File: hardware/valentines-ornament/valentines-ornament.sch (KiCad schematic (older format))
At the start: 17 parts, among them U1 ATtiny85-20SU

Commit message: Finished schematic capture; started PCB layout
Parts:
- added C1: 10uF, Capacitors_SMD:C_1206_HandSoldering, symbol Device:C
- added J1: AVR-ISP-6, Pin_Headers:Pin_Header_Straight_2x03_Pitch2.54mm_SMD, symbol Connector:AVR-ISP-6
- added R5: 10K, Resistors_SMD:R_1206_HandSoldering, symbol Device:R
- added SW1: SW_Push, Buttons_Switches_SMD:SW_SPST_EVQQ2, symbol Switch:SW_Push
- U1: footprint Package_SO:SOIJ-8_5.3x5.3mm_P1.27mm -> kicad-libs:SOIJ-8_5.3x5.3mm_P1.27mm
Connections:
- net RST: now reaches U1.1 (~RESET~/PB5)
- net RST: now also J1.5 (~RST)
- net at U1.2 (XTAL1/PB3): now also R3.2
- net at U1.3 (XTAL2/PB4): now also R4.2
- net GND: now reaches U1.4 (GND)
- net GND: now also C1.1, J1.6 (GND), R5.2
- net MOSI: now reaches U1.5 (AREF/PB0)
- net MOSI: now also R1.2, J1.4 (MOSI)
- net MISO: now reaches U1.6 (PB1)
- net MISO: now also R2.2, J1.1 (MISO)
- net SCK_BUTTON: now reaches U1.7 (PB2)
- net SCK_BUTTON: now also J1.3 (SCK), R5.1, SW1.2
- net +3V3: now reaches U1.8 (VCC)
- net +3V3: now also C1.2, J1.2 (VCC), SW1.1
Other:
- moved on the sheet: D1, D10, D11, D12, D2, D3, D4, D5, D6, D7, D8, D9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

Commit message: Add battery cell
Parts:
- added BT1: Battery_Cell, kicad-libs:CR2032-SMD, symbol Device:Battery_Cell
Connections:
- net +3V3: now also BT1.1 (+)
- net GND: now also BT1.2 (-)
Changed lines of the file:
@@
 	4700 3550 5200 3550
 $Comp
-L power:PWR_FLAG #FLG?
+L power:PWR_FLAG #FLG0101
 U 1 1 5C577048
 P 2150 4700
-F 0 "#FLG?" H 2150 4775 50  0001 C CNN
+F 0 "#FLG0101" H 2150 4775 50  0001 C CNN
 F 1 "PWR_FLAG" V 2150 4828 50  0000 L CNN
 F 2 "" H 2150 4700 50  0001 C CNN
@@
 Connection ~ 2150 4700
 $Comp
-L power:PWR_FLAG #FLG?
+L power:PWR_FLAG #FLG0102
 U 1 1 5C5770B0
 P 2150 5600
-F 0 "#FLG?" H 2150 5675 50  0001 C CNN
+F 0 "#FLG0102" H 2150 5675 50  0001 C CNN
 F 1 "PWR_FLAG" V 2150 5728 50  0000 L CNN
 F 2 "" H 2150 5600 50  0001 C CNN
@@
 $EndComp
 Connection ~ 2150 5600
+$Comp
+L Device:Battery_Cell BT1
+U 1 1 5C57A79D
+P 1800 2150
+F 0 "BT1" H 1918 2246 50  0000 L CNN
+F 1 "Battery_Cell" H 1918 2155 50  0000 L CNN
+F 2 "kicad-libs:CR2032-SMD" V 1800 2210 50  0001 C CNN
+F 3 "~" V 1800 2210 50  0001 C CNN
+	1    1800 2150
+	1    0    0    -1
+$EndComp
+$Comp
+L power:+3.3V #PWR0108
+U 1 1 5C57AA3C
+P 1800 1950
+F 0 "#PWR0108" H 1800 1800 50  0001 C CNN
+F 1 "+3.3V" H 1815 2123 50  0000 C CNN
+F 2 "" H 1800 1950 50  0001 C CNN
+F 3 "" H 1800 1950 50  0001 C CNN
+	1    1800 1950
+	1    0    0    -1
+$EndComp
+$Comp
+L power:GND #PWR0109
+U 1 1 5C57AAB4
+P 1800 2250
+F 0 "#PWR0109" H 1800 2000 50  0001 C CNN
+F 1 "GND" H 1805 2077 50  0000 C CNN
+F 2 "" H 1800 2250 50  0001 C CNN
+F 3 "" H 1800 2250 50  0001 C CNN
+	1    1800 2250
+	1    0    0    -1
+$EndComp
 $EndSCHEMATC

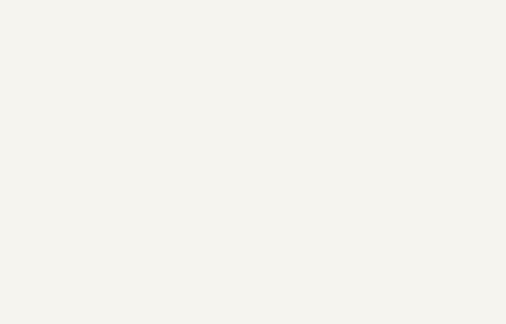
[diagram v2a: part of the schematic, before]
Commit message: Add heart solder mask logo, switch resistors to 0805
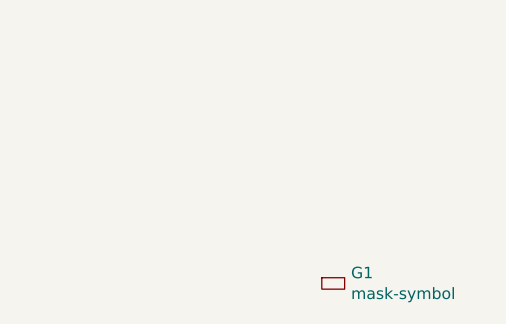
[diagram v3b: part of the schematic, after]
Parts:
- added G1: mask-symbol, kicad-libs:abstract-heart, symbol petezah:mask-symbol
- R1, R2, R3, R4, R5: footprint Resistors_SMD:R_1206_HandSoldering -> Resistors_SMD:R_0805_HandSoldering
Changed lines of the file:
@@
 F 0 "R1" V 5143 2350 50  0000 C CNN
 F 1 "270" V 5234 2350 50  0000 C CNN
-F 2 "Resistors_SMD:R_1206_HandSoldering" V 5280 2350 50  0001 C CNN
+F 2 "Resistors_SMD:R_0805_HandSoldering" V 5280 2350 50  0001 C CNN
 F 3 "~" H 5350 2350 50  0001 C CNN
 	1    5350 2350
@@
 F 0 "R2" V 5143 2750 50  0000 C CNN
 F 1 "270" V 5234 2750 50  0000 C CNN
-F 2 "Resistors_SMD:R_1206_HandSoldering" V 5280 2750 50  0001 C CNN
+F 2 "Resistors_SMD:R_0805_HandSoldering" V 5280 2750 50  0001 C CNN
 F 3 "~" H 5350 2750 50  0001 C CNN
 	1    5350 2750
@@
 F 0 "R3" V 5143 3150 50  0000 C CNN
 F 1 "270" V 5234 3150 50  0000 C CNN
-F 2 "Resistors_SMD:R_1206_HandSoldering" V 5280 3150 50  0001 C CNN
+F 2 "Resistors_SMD:R_0805_HandSoldering" V 5280 3150 50  0001 C CNN
 F 3 "~" H 5350 3150 50  0001 C CNN
 	1    5350 3150
@@
 F 0 "R4" V 5143 3550 50  0000 C CNN
 F 1 "270" V 5234 3550 50  0000 C CNN
-F 2 "Resistors_SMD:R_1206_HandSoldering" V 5280 3550 50  0001 C CNN
+F 2 "Resistors_SMD:R_0805_HandSoldering" V 5280 3550 50  0001 C CNN
 F 3 "~" H 5350 3550 50  0001 C CNN
 	1    5350 3550
@@
 F 0 "R5" H 5170 5096 50  0000 L CNN
 F 1 "10K" H 5170 5005 50  0000 L CNN
-F 2 "Resistors_SMD:R_1206_HandSoldering" V 5030 5050 50  0001 C CNN
+F 2 "Resistors_SMD:R_0805_HandSoldering" V 5030 5050 50  0001 C CNN
 F 3 "~" H 5100 5050 50  0001 C CNN
 	1    5100 5050
@@
 	1    0    0    -1
 $EndComp
+$Comp
+L petezah:mask-symbol G1
+U 1 1 5C58D7F8
+P 9150 6850
+F 0 "G1" H 9228 6921 50  0000 L CNN
+F 1 "mask-symbol" H 9228 6830 50  0000 L CNN
+F 2 "kicad-libs:abstract-heart" H 9150 7000 50  0001 C CNN
+F 3 "" H 9150 7000 50  0001 C CNN
+	1    9150 6850
+	1    0    0    -1
+$EndComp

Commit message: Finish placing
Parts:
- added H1, H2: MountingHole, Mounting_Holes:MountingHole_2.2mm_M2, symbol Mechanical:MountingHole
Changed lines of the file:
@@
+	1    0    0    -1
+$EndComp
+$Comp
+L Mechanical:MountingHole H1
+U 1 1 5C58F77A
+P 10150 6700
+F 0 "H1" H 10250 6746 50  0000 L CNN
+F 1 "MountingHole" H 10250 6655 50  0000 L CNN
+F 2 "Mounting_Holes:MountingHole_2.2mm_M2" H 10150 6700 50  0001 C CNN
+F 3 "~" H 10150 6700 50  0001 C CNN
+	1    10150 6700
+	1    0    0    -1
+$EndComp
+$Comp
+L Mechanical:MountingHole H2
+U 1 1 5C58F817
+P 10150 6950
+F 0 "H2" H 10250 6996 50  0000 L CNN
+F 1 "MountingHole" H 10250 6905 50  0000 L CNN
+F 2 "Mounting_Holes:MountingHole_2.2mm_M2" H 10150 6950 50  0001 C CNN
+F 3 "~" H 10150 6950 50  0001 C CNN
+	1    10150 6950
 	1    0    0    -1
 $EndComp
